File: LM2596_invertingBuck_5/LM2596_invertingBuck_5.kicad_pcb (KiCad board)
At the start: 2 copper layers, 62 x 39 mm, 10 parts, among them J1 Input, J2 Output, Q1 2N3904, U1 LM2596T-5

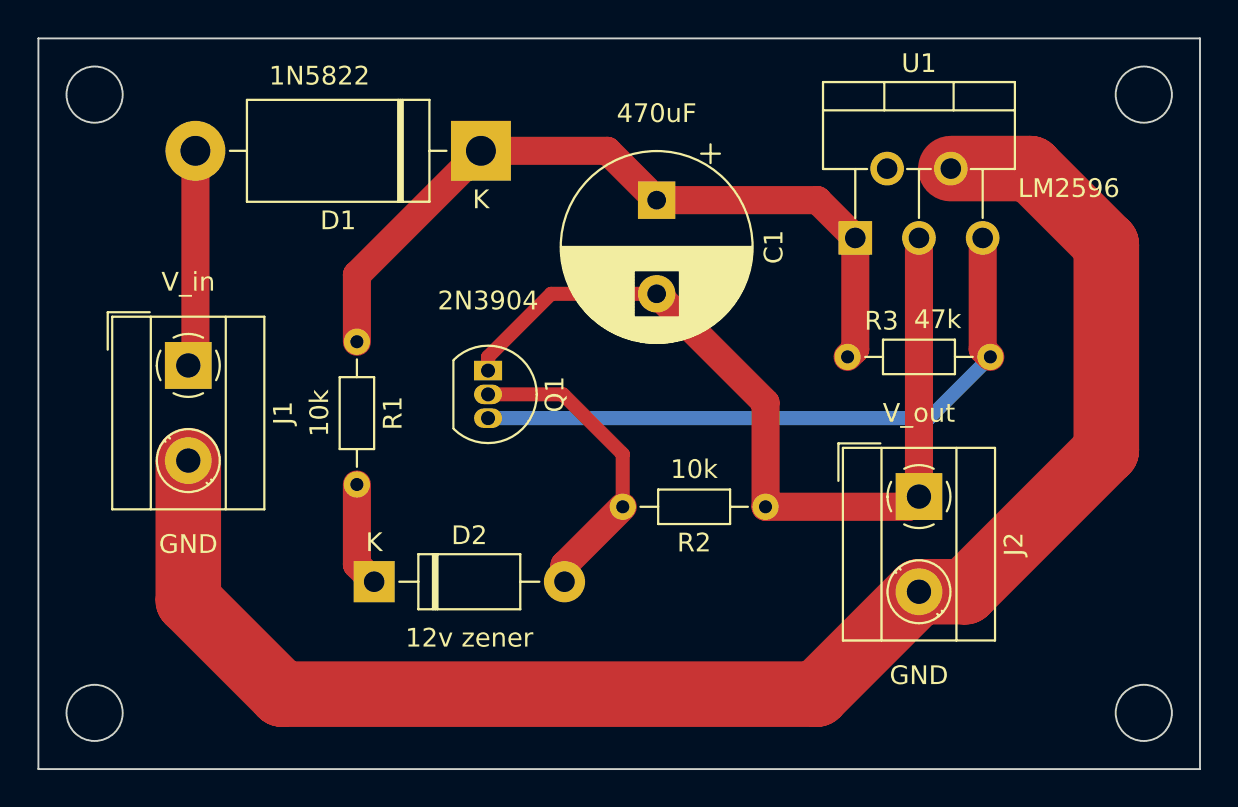
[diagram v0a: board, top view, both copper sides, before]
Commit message: improve inverting buk design
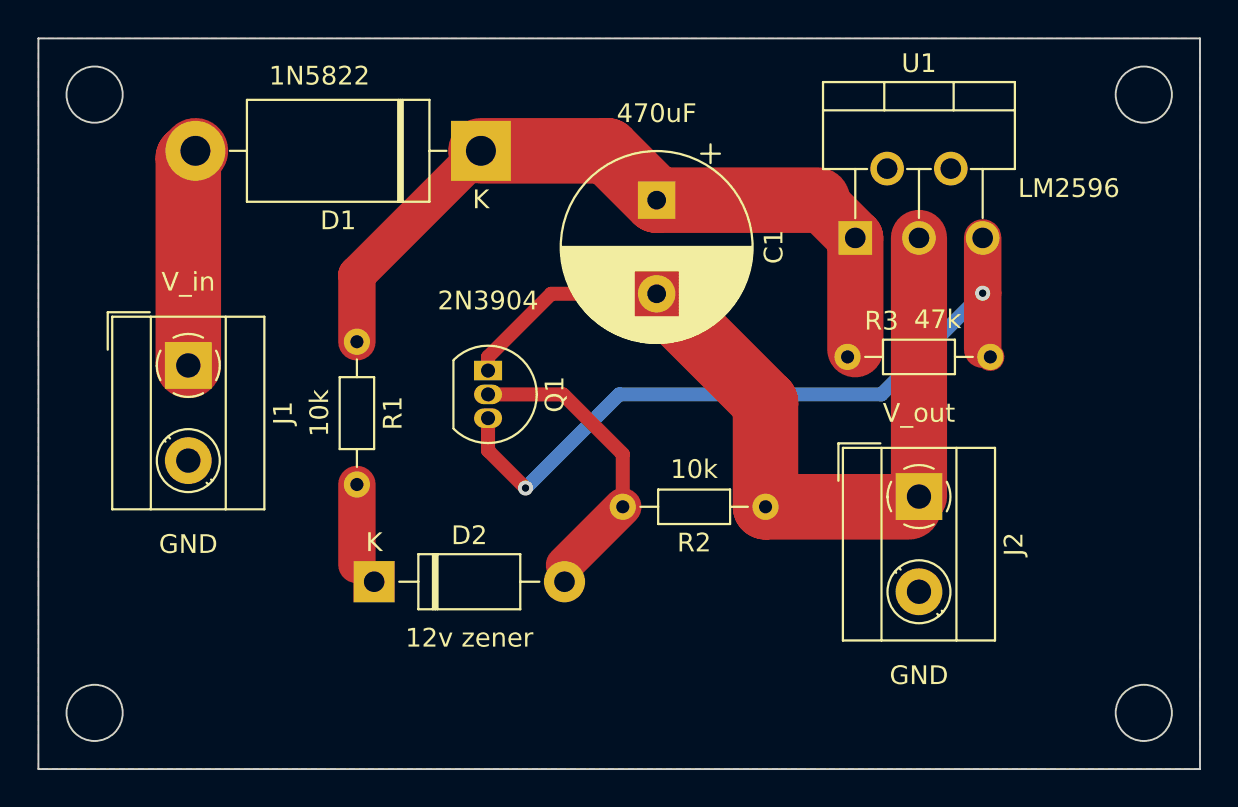
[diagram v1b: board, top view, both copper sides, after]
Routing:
- net GND: track 84.9 -> 0.00 mm
- net Net-(Q1-Pad3): track 34.7 -> 39.8 mm, vias 0 -> 2
- added copper zone on F.Cu, net GND
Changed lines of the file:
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@@
     (effects (font (size 1 1) (thickness 0.15)))
   )
-  (segment (start 130.582323 76.632323) (end 132.6 78.65) (width 1.5) (layer "F.Cu") (net 1))
-  (segment (start 106 84.19) (end 106 80.62) (width 1.5) (layer "F.Cu") (net 1))
-  (segment (start 122 76.632323) (end 130.582323 76.632323) (width 1.5) (layer "F.Cu") (net 1))
+  (segment (start 130.582323 76.632323) (end 132.6 78.65) (width 3) (layer "F.Cu") (net 1))
+  (segment (start 106 84.19) (end 106 80.62) (width 2) (layer "F.Cu") (net 1))
+  (segment (start 122 76.632323) (end 130.582323 76.632323) (width 3.5) (layer "F.Cu") (net 1))
   (segment (start 132.6 84.59) (end 132.19 85) (width 1.5) (layer "F.Cu") (net 1))
-  (segment (start 132.6 78.65) (end 132.6 84.59) (width 1.5) (layer "F.Cu") (net 1))
-  (segment (start 106 80.62) (end 112.62 74) (width 1.5) (layer "F.Cu") (net 1))
-  (segment (start 112.62 74) (end 119.367677 74) (width 1.5) (layer "F.Cu") (net 1))
-  (segment (start 119.367677 74) (end 122 76.632323) (width 1.5) (layer "F.Cu") (net 1))
+  (segment (start 132.6 78.65) (end 132.6 84.59) (width 3) (layer "F.Cu") (net 1))
+  (segment (start 106 80.62) (end 112.62 74) (width 2) (layer "F.Cu") (net 1))
+  (segment (start 112.62 74) (end 119.367677 74) (width 3.5) (layer "F.Cu") (net 1))
+  (segment (start 119.367677 74) (end 122 76.632323) (width 3.5) (layer "F.Cu") (net 1))
   (segment (start 113 85.73) (end 113 85) (width 0.75) (layer "F.Cu") (net 2))
-  (segment (start 127.81 93) (end 127.81 87.442323) (width 1.5) (layer "F.Cu") (net 2))
+  (segment (start 127.81 93) (end 127.81 87.442323) (width 3.5) (layer "F.Cu") (net 2))
   (segment (start 135.455 93) (end 136 92.455) (width 1.5) (layer "F.Cu") (net 2))
-  (segment (start 127.81 87.442323) (end 122 81.632323) (width 1.5) (layer "F.Cu") (net 2))
-  (segment (start 127.81 93) (end 135.455 93) (width 1.5) (layer "F.Cu") (net 2))
+  (segment (start 127.81 87.442323) (end 122 81.632323) (width 3.5) (layer "F.Cu") (net 2))
+  (segment (start 127.81 93) (end 135.455 93) (width 3.5) (layer "F.Cu") (net 2))
   (segment (start 116.367677 81.632323) (end 122 81.632323) (width 0.75) (layer "F.Cu") (net 2))
   (segment (start 113 85) (end 116.367677 81.632323) (width 0.75) (layer "F.Cu") (net 2))
-  (segment (start 136 92.455) (end 136 78.65) (width 1.5) (layer "F.Cu") (net 2))
-  (segment (start 97.38 85.075) (end 97 85.455) (width 1.5) (layer "F.Cu") (net 3))
-  (segment (start 97.38 74) (end 97.38 85.075) (width 1.5) (layer "F.Cu") (net 3))
-  (segment (start 106 91.81) (end 106 96.08) (width 1.5) (layer "F.Cu") (net 4))
+  (segment (start 136 92.455) (end 136 78.65) (width 3) (layer "F.Cu") (net 2))
+  (segment (start 97 85.455) (end 97 74.38) (width 3.5) (layer "F.Cu") (net 3))
+  (segment (start 97 74.38) (end 97.38 74) (width 3.5) (layer "F.Cu") (net 3))
+  (segment (start 106 91.81) (end 106 96.08) (width 2) (layer "F.Cu") (net 4))
   (segment (start 106 96.08) (end 106.92 97) (width 1.5) (layer "F.Cu") (net 4))
   (segment (start 117.08 97) (end 117.08 96.11) (width 1.5) (layer "F.Cu") (net 5))
@@
   (segment (start 117 87) (end 120.19 90.19) (width 0.75) (layer "F.Cu") (net 5))
   (segment (start 113 87) (end 117 87) (width 0.75) (layer "F.Cu") (net 5))
-  (segment (start 117.08 96.11) (end 120.19 93) (width 1.5) (layer "F.Cu") (net 5))
-  (segment (start 146 90) (end 138.465 97.535) (width 3.5) (layer "F.Cu") (net 6))
-  (segment (start 137.7 74.95) (end 141.95 74.95) (width 3.5) (layer "F.Cu") (net 6))
-  (segment (start 146 79) (end 146 90) (width 3.5) (layer "F.Cu") (net 6))
-  (segment (start 138.465 97.535) (end 136 97.535) (width 3.5) (layer "F.Cu") (net 6))
-  (segment (start 97 90.535) (end 97 98) (width 3.5) (layer "F.Cu") (net 6))
-  (segment (start 141.95 74.95) (end 146 79) (width 3.5) (layer "F.Cu") (net 6))
-  (segment (start 97 98) (end 102 103) (width 3.5) (layer "F.Cu") (net 6))
-  (segment (start 130.535 103) (end 136 97.535) (width 3.5) (layer "F.Cu") (net 6))
-  (segment (start 102 103) (end 130.535 103) (width 3.5) (layer "F.Cu") (net 6))
-  (segment (start 139.4 78.65) (end 139.4 84.59) (width 1.5) (layer "F.Cu") (net 7))
+  (segment (start 117.08 96.11) (end 120.19 93) (width 2) (layer "F.Cu") (net 5))
+  (segment (start 139.4 78.65) (end 139.4 81.6) (width 2) (layer "F.Cu") (net 7))
   (segment (start 139.4 84.59) (end 139.81 85) (width 1.5) (layer "F.Cu") (net 7))
-  (segment (start 113 88.27) (end 136.54 88.27) (width 0.75) (layer "B.Cu") (net 7))
-  (segment (start 136.54 88.27) (end 139.81 85) (width 0.75) (layer "B.Cu") (net 7))
+  (segment (start 113 90) (end 115 92) (width 0.75) (layer "F.Cu") (net 7))
+  (segment (start 113 88.27) (end 113 90) (width 0.75) (layer "F.Cu") (net 7))
+  (segment (start 139.4 81.6) (end 139.4 84.59) (width 2) (layer "F.Cu") (net 7))
+  (via (at 115 92) (size 0.8) (drill 0.4) (layers "F.Cu" "B.Cu") (net 7))
+  (via (at 139.4 81.6) (size 0.8) (drill 0.4) (layers "F.Cu" "B.Cu") (net 7))
+  (segment (start 120 87) (end 134 87) (width 0.75) (layer "B.Cu") (net 7))
+  (segment (start 134 87) (end 139.4 81.6) (width 0.75) (layer "B.Cu") (net 7))
+  (segment (start 115 92) (end 120 87) (width 0.75) (layer "B.Cu") (net 7))
+  (zone (net 6) (net_name "GND") (layer "F.Cu") (hatch edge 0.508)
+    (connect_pads (clearance 0.508))
+    (min_thickness 0.254) (filled_areas_thickness no)
+    (fill yes (thermal_gap 0.508) (thermal_bridge_width 0.508))
+    (polygon
+      (pts
+        (xy 151 107)
+        (xy 89 107)
+        (xy 89 68)
+        (xy 151 68)
+      )
+    )
+  )
 )
